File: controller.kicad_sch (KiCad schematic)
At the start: 12 parts, among them J2 Debug, SW4 RST, U10 STM32C031K6Tx

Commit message: Controller component value assignment
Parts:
- C13: value C -> 4.7u
- C14, C15: value C -> 100n
- R3, R31, R32, R4: value R -> 5k6
- R5: value R -> 220
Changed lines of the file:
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@@
 			)
 		)
-		(property "Value" "R"
+		(property "Value" "5k6"
 			(at 217.932 27.94 90)
 			(effects
@@
 			)
 		)
-		(property "Value" "R"
+		(property "Value" "220"
 			(at 169.672 130.81 90)
 			(effects
@@
 			)
 		)
-		(property "Value" "R"
+		(property "Value" "5k6"
 			(at 106.172 39.37 90)
 			(effects
@@
 			)
 		)
-		(property "Value" "C"
+		(property "Value" "4.7u"
 			(at 118.11 66.0399 0)
 			(effects
@@
 			)
 		)
-		(property "Value" "C"
+		(property "Value" "100n"
 			(at 130.81 66.0399 0)
 			(effects
@@
 			)
 		)
-		(property "Value" "C"
+		(property "Value" "100n"
 			(at 67.31 83.8199 0)
 			(effects
@@
 			)
 		)
-		(property "Value" "R"
+		(property "Value" "5k6"
 			(at 98.552 39.37 90)
 			(effects
@@
 			)
 		)
-		(property "Value" "R"
+		(property "Value" "5k6"
 			(at 210.312 27.94 90)
 			(effects

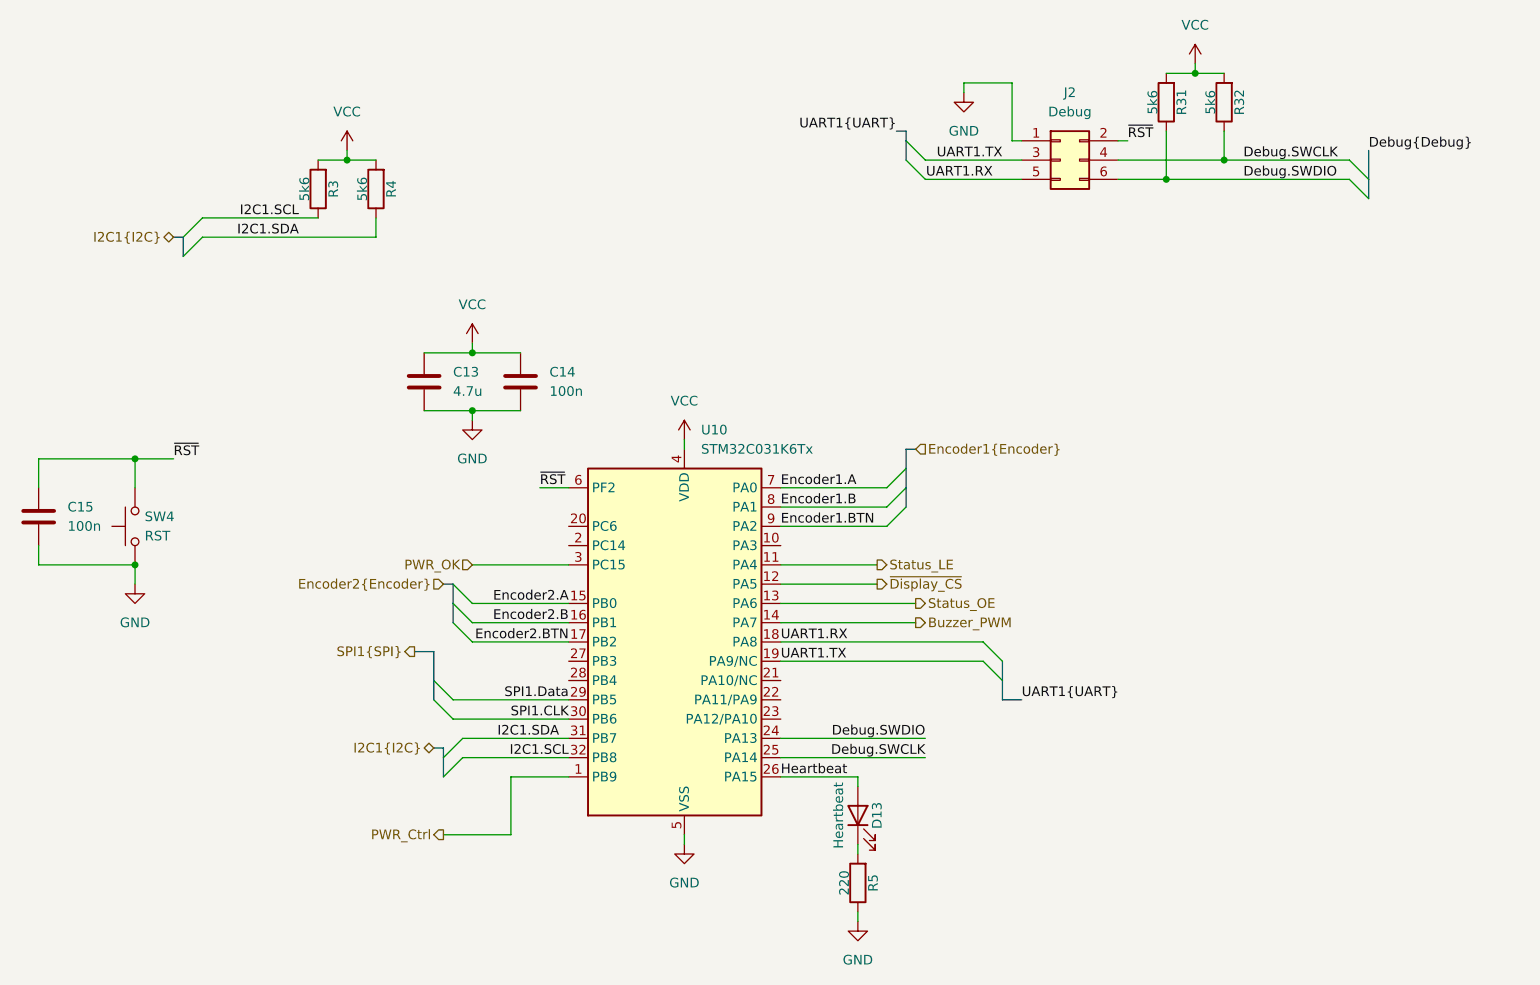
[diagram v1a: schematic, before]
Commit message: Resolve ERC warnings
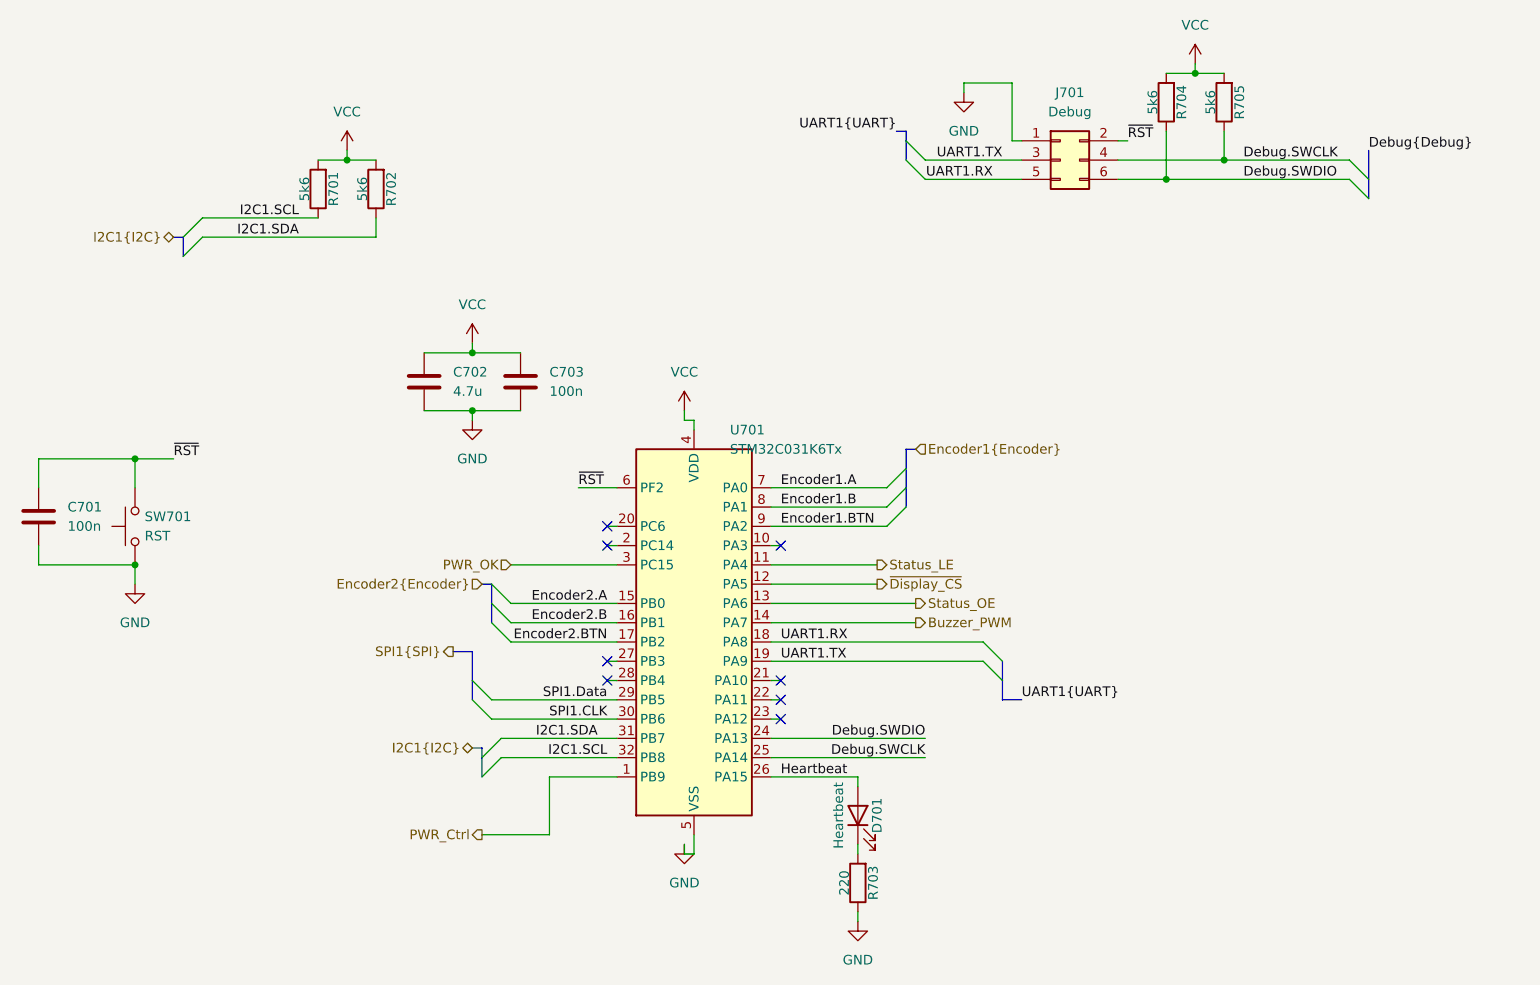
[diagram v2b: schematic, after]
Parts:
- renumbered C15 to C701, C13 to C702, C14 to C703, D13 to D701, J2 to J701, R3 to R701, R4 to R702, R5 to R703, R31 to R704, R32 to R705, SW4 to SW701, U10 to U701
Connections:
- no-connect marks 0 -> 8
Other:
- moved on the sheet: U701

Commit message: Add Testpoints
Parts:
- added R706: 10k, Resistor_SMD:R_0805_2012Metric_Pad1.20x1.40mm_HandSolder, symbol Device:R
- added TP15: CLK, symbol Connector:TestPoint
- added TP16: DATA, symbol Connector:TestPoint
- added TP17: SDA, symbol Connector:TestPoint
- added TP18: SCL, symbol Connector:TestPoint
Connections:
- net I2C1.SCL: now also TP18.1
- net I2C1.SDA: now also TP17.1
- net SPI1.CLK: now also TP15.1
- net SPI1.Data: now also TP16.1
- net VCC: now also R706.2
- net ~{RST}: now also R706.1

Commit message: Footprint selection
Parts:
- C701, C702, C703: footprint Capacitor_SMD:C_0805_2012Metric_Pad1.18x1.45mm_HandSolder -> Capacitor_SMD:C_1206_3216Metric_Pad1.33x1.80mm_HandSolder
- D701: footprint LED_SMD:LED_0805_2012Metric_Pad1.15x1.40mm_HandSolder -> LED_SMD:LED_1206_3216Metric_Pad1.42x1.75mm_HandSolder
- R701, R702, R703, R704, R705, R706: footprint Resistor_SMD:R_0805_2012Metric_Pad1.20x1.40mm_HandSolder -> Resistor_SMD:R_1206_3216Metric_Pad1.30x1.75mm_HandSolder
- TP15, TP16, TP17, TP18: footprint (none) -> TestPoint:TestPoint_Pad_D1.0mm
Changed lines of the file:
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@@
 			)
 		)
-		(property "Footprint" "Resistor_SMD:R_0805_2012Metric_Pad1.20x1.40mm_HandSolder"
+		(property "Footprint" "Resistor_SMD:R_1206_3216Metric_Pad1.30x1.75mm_HandSolder"
 			(at 221.488 27.94 90)
 			(effects
@@
 			)
 		)
-		(property "Footprint" ""
+		(property "Footprint" "TestPoint:TestPoint_Pad_D1.0mm"
 			(at 91.44 43.18 0)
 			(effects
@@
 			)
 		)
-		(property "Footprint" "Resistor_SMD:R_0805_2012Metric_Pad1.20x1.40mm_HandSolder"
+		(property "Footprint" "Resistor_SMD:R_1206_3216Metric_Pad1.30x1.75mm_HandSolder"
 			(at 173.228 130.81 90)
 			(effects
@@
 			)
 		)
-		(property "Footprint" "Resistor_SMD:R_0805_2012Metric_Pad1.20x1.40mm_HandSolder"
+		(property "Footprint" "Resistor_SMD:R_1206_3216Metric_Pad1.30x1.75mm_HandSolder"
 			(at 109.728 39.37 90)
 			(effects
@@
 			)
 		)
-		(property "Footprint" ""
+		(property "Footprint" "TestPoint:TestPoint_Pad_D1.0mm"
 			(at 229.87 74.93 0)
 			(effects
@@
 			)
 		)
-		(property "Footprint" "Capacitor_SMD:C_0805_2012Metric_Pad1.18x1.45mm_HandSolder"
+		(property "Footprint" "Capacitor_SMD:C_1206_3216Metric_Pad1.33x1.80mm_HandSolder"
 			(at 115.2652 68.58 0)
 			(effects
@@
 			)
 		)
-		(property "Footprint" ""
+		(property "Footprint" "TestPoint:TestPoint_Pad_D1.0mm"
 			(at 96.52 45.72 0)
 			(effects
@@
 			)
 		)
-		(property "Footprint" "Capacitor_SMD:C_0805_2012Metric_Pad1.18x1.45mm_HandSolder"
+		(property "Footprint" "Capacitor_SMD:C_1206_3216Metric_Pad1.33x1.80mm_HandSolder"
 			(at 127.9652 68.58 0)
 			(effects
@@
 			)
 		)
-		(property "Footprint" ""
+		(property "Footprint" "TestPoint:TestPoint_Pad_D1.0mm"
 			(at 240.03 72.39 0)
 			(effects
@@
 			)
 		)
-		(property "Footprint" "Capacitor_SMD:C_0805_2012Metric_Pad1.18x1.45mm_HandSolder"
+		(property "Footprint" "Capacitor_SMD:C_1206_3216Metric_Pad1.33x1.80mm_HandSolder"
 			(at 64.4652 86.36 0)
 			(effects
@@
 			)
 		)
-		(property "Footprint" "Resistor_SMD:R_0805_2012Metric_Pad1.20x1.40mm_HandSolder"
+		(property "Footprint" "Resistor_SMD:R_1206_3216Metric_Pad1.30x1.75mm_HandSolder"
 			(at 65.278 69.85 90)
 			(effects
@@
 			)
 		)
-		(property "Footprint" "Resistor_SMD:R_0805_2012Metric_Pad1.20x1.40mm_HandSolder"
+		(property "Footprint" "Resistor_SMD:R_1206_3216Metric_Pad1.30x1.75mm_HandSolder"
 			(at 102.108 39.37 90)
 			(effects
@@
 			)
 		)
-		(property "Footprint" "LED_SMD:LED_0805_2012Metric_Pad1.15x1.40mm_HandSolder"
+		(property "Footprint" "LED_SMD:LED_1206_3216Metric_Pad1.42x1.75mm_HandSolder"
 			(at 171.45 121.92 0)
 			(effects
@@
 			)
 		)
-		(property "Footprint" "Resistor_SMD:R_0805_2012Metric_Pad1.20x1.40mm_HandSolder"
+		(property "Footprint" "Resistor_SMD:R_1206_3216Metric_Pad1.30x1.75mm_HandSolder"
 			(at 213.868 27.94 90)
 			(effects
